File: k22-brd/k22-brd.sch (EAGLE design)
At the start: 35 parts, among them J1 61302011121, J2 61302011121, J3 CORTEX_DEBUG_PTH

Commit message: Vetsi text
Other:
- note added: "B PTD4 BTN"
- note added: "L PTD5 LED"
- note added: "R Reset BTN"
- note added: "U USB connector"
- note removed: "PTD4 BTN"
- note removed: "PTD5 LED"
- note removed: "Reset BTN"
- note removed: "USB connector"
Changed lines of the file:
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@@
 <setting verticaltext="up"/>
 </settings>
-<grid distance="0.1" unitdist="inch" unit="inch" style="lines" multiple="1" display="no" altdistance="0.01" altunitdist="inch" altunit="inch"/>
+<grid distance="0.1" unitdist="inch" unit="mm" style="lines" multiple="1" display="no" altdistance="0.01" altunitdist="inch" altunit="inch"/>
 <layers>
 <layer number="1" name="Top" color="4" fill="1" visible="no" active="no"/>
@@
 <sheet>
 <plain>
-<text x="185.42" y="43.18" size="1.778" layer="104">S SWD Connector</text>
-<text x="177.8" y="-25.4" size="1.778" layer="247">PTD5 LED</text>
-<text x="45.72" y="-25.4" size="1.778" layer="247">Reset BTN</text>
-<text x="-68.58" y="76.2" size="1.778" layer="247">USB connector</text>
-<text x="-68.58" y="129.54" size="1.778" layer="247">V Voltage regulator</text>
-<text x="45.72" y="129.54" size="1.778" layer="247">M MCU</text>
-<text x="177.8" y="129.54" size="1.778" layer="247">Connectors</text>
+<text x="185.42" y="43.18" size="2.54" layer="247">S SWD Connector</text>
+<text x="177.8" y="-25.4" size="2.54" layer="247">L PTD5 LED</text>
+<text x="45.72" y="-25.4" size="2.54" layer="247">R Reset BTN</text>
+<text x="-68.58" y="76.2" size="2.54" layer="247">U USB connector</text>
+<text x="-68.58" y="129.54" size="2.54" layer="247">V Voltage regulator</text>
+<text x="45.72" y="129.54" size="2.54" layer="247">M MCU</text>
+<text x="177.8" y="129.54" size="2.54" layer="247">Connectors</text>
 <wire x1="43.18" y1="-20.32" x2="43.18" y2="-53.34" width="0.1524" layer="247"/>
 <wire x1="43.18" y1="-53.34" x2="101.6" y2="-53.34" width="0.1524" layer="247"/>
@@
 <wire x1="106.68" y1="-53.34" x2="167.64" y2="-53.34" width="0.1524" layer="247"/>
 <wire x1="106.68" y1="-20.32" x2="167.64" y2="-20.32" width="0.1524" layer="247"/>
-<text x="109.22" y="-25.4" size="1.778" layer="247">PTD4 BTN</text>
+<text x="109.22" y="-25.4" size="2.54" layer="247">B PTD4 BTN</text>
 <wire x1="175.26" y1="-20.32" x2="175.26" y2="-53.34" width="0.1524" layer="247"/>
 <wire x1="175.26" y1="-53.34" x2="231.14" y2="-53.34" width="0.1524" layer="247"/>

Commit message: overlap, crystal pad, usb pad, bead pad
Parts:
- removed LU1, LU2: 330, rcl:L-EUL2012C
- added FBU1, FBU2: 330, BeagleBone_Black_Wireless:GHI-BASICCOMPONENTS_FB-(INCH)-0805
- USB-C: device Eagle_WR-USB (rev22b):629722000214 -> poli-USB-C:629722000214
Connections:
- net GND: now also FBU2.P$2; no longer LU2.1
- net USB5V: now also FBU1.P$2; no longer LU1.1
- net USBGNDSHIELD: now also FBU2.P$1; no longer LU2.2
- net VBUSCON: now also FBU1.P$1; no longer LU1.2
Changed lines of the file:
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@@
 <setting verticaltext="up"/>
 </settings>
-<grid distance="0.1" unitdist="inch" unit="mm" style="lines" multiple="1" display="no" altdistance="0.01" altunitdist="inch" altunit="inch"/>
+<grid distance="0.1" unitdist="inch" unit="inch" style="lines" multiple="1" display="no" altdistance="0.01" altunitdist="inch" altunit="inch"/>
 <layers>
 <layer number="1" name="Top" color="4" fill="1" visible="no" active="no"/>
@@
 <part name="J1" library="Headers" library_urn="urn:adsk.eagle:library:11687645" deviceset="61302011121" device="" package3d_urn="urn:adsk.eagle:package:11391910/2"/>
 <part name="J2" library="Headers" library_urn="urn:adsk.eagle:library:11687645" deviceset="61302011121" device="" package3d_urn="urn:adsk.eagle:package:11391910/2"/>
-<part name="USB-C" library="Eagle_WR-USB (rev22b)" deviceset="629722000214" device="" package3d_urn="urn:adsk.eagle:package:32827710/4" value="629722000214"/>
-<part name="LU1" library="rcl" library_urn="urn:adsk.eagle:library:334" deviceset="L-EU" device="L2012C" package3d_urn="urn:adsk.eagle:package:23475/2" value="330"/>
-<part name="LU2" library="rcl" library_urn="urn:adsk.eagle:library:334" deviceset="L-EU" device="L2012C" package3d_urn="urn:adsk.eagle:package:23475/2" value="330"/>
+<part name="USB-C" library="poli-USB-C" deviceset="629722000214" device="" package3d_urn="urn:adsk.eagle:package:32827710/4" value="629722000214"/>
 <part name="RU1" library="rcl" library_urn="urn:adsk.eagle:library:334" deviceset="R-EU_" device="R0805" package3d_urn="urn:adsk.eagle:package:23553/2" value="5k1"/>
 <part name="RU2" library="rcl" library_urn="urn:adsk.eagle:library:334" deviceset="R-EU_" device="R0805" package3d_urn="urn:adsk.eagle:package:23553/2" value="5k1"/>
@@
 <part name="U$5" library="vym0038_k22_misc" deviceset="USBLC6-2SC6" device=""/>
 <part name="CU1" library="rcl" library_urn="urn:adsk.eagle:library:334" deviceset="C-EU" device="C0805" package3d_urn="urn:adsk.eagle:package:23617/2" value="&lt;1,10&gt;u"/>
+<part name="FBU1" library="BeagleBone_Black_Wireless" library_urn="urn:adsk.eagle:library:6644236" deviceset="GHI-BASICCOMPONENTS_FB-(INCH)-" device="0805" package3d_urn="urn:adsk.eagle:package:6644355/2" value="330"/>
+<part name="FBU2" library="BeagleBone_Black_Wireless" library_urn="urn:adsk.eagle:library:6644236" deviceset="GHI-BASICCOMPONENTS_FB-(INCH)-" device="0805" package3d_urn="urn:adsk.eagle:package:6644355/2" value="330"/>
 </parts>
 <sheets>
@@
 <attribute name="VALUE" x="-17.78" y="10.16" size="1.6764" layer="96" align="bottom-center"/>
 </instance>
-<instance part="LU1" gate="G$1" x="-33.02" y="50.8" smashed="yes" rot="R270">
-<attribute name="NAME" x="-36.83" y="52.2986" size="1.778" layer="95"/>
-<attribute name="VALUE" x="-36.83" y="47.498" size="1.778" layer="96"/>
-</instance>
-<instance part="LU2" gate="G$1" x="-33.02" y="43.18" smashed="yes" rot="R270">
-<attribute name="NAME" x="-36.83" y="44.6786" size="1.778" layer="95"/>
-<attribute name="VALUE" x="-36.83" y="39.878" size="1.778" layer="96"/>
-</instance>
 <instance part="RU1" gate="G$1" x="2.54" y="50.8" smashed="yes">
 <attribute name="NAME" x="-1.27" y="52.2986" size="1.778" layer="95"/>
@@
 <attribute name="NAME" x="-33.401" y="59.944" size="1.778" layer="95" rot="R90"/>
 <attribute name="VALUE" x="-28.321" y="59.944" size="1.778" layer="96" rot="R90"/>
+</instance>
+<instance part="FBU1" gate="G$1" x="-33.02" y="50.8" smashed="yes">
+<attribute name="NAME" x="-36.195" y="52.705" size="1.778" layer="95"/>
+<attribute name="VALUE" x="-36.195" y="46.99" size="1.778" layer="96"/>
+</instance>
+<instance part="FBU2" gate="G$1" x="-33.02" y="43.18" smashed="yes">
+<attribute name="NAME" x="-36.195" y="45.085" size="1.778" layer="95"/>
+<attribute name="VALUE" x="-36.195" y="39.37" size="1.778" layer="96"/>
 </instance>
 </instances>
@@
 </segment>
 <segment>
-<pinref part="LU2" gate="G$1" pin="1"/>
 <wire x1="-20.32" y1="43.18" x2="-27.94" y2="43.18" width="0.1524" layer="91"/>
 <label x="-25.4" y="43.18" size="1.778" layer="95"/>
+<pinref part="FBU2" gate="G$1" pin="P$2"/>
 </segment>
 <segment>
@@
 </segment>
 <segment>
-<pinref part="LU1" gate="G$1" pin="2"/>
 <wire x1="-45.72" y1="50.8" x2="-38.1" y2="50.8" width="0.1524" layer="91"/>
 <label x="-50.8" y="50.8" size="1.778" layer="95"/>
+<pinref part="FBU1" gate="G$1" pin="P$1"/>
 </segment>
 <segment>
@@
 </segment>
 <segment>
-<pinref part="LU2" gate="G$1" pin="2"/>
 <wire x1="-45.72" y1="43.18" x2="-38.1" y2="43.18" width="0.1524" layer="91"/>
 <label x="-58.42" y="43.18" size="1.778" layer="95"/>
+<pinref part="FBU2" gate="G$1" pin="P$1"/>
 </segment>
 </net>
@@
 <net name="USB5V" class="0">
 <segment>
-<pinref part="LU1" gate="G$1" pin="1"/>
 <wire x1="-27.94" y1="50.8" x2="-20.32" y2="50.8" width="0.1524" layer="91"/>
 <label x="-25.4" y="50.8" size="1.778" layer="95"/>
@@
 <wire x1="-27.94" y1="50.8" x2="-27.94" y2="58.42" width="0.1524" layer="91"/>
 <junction x="-27.94" y="50.8"/>
-</segment>
-<segment>
+<pinref part="FBU1" gate="G$1" pin="P$2"/>
+</segment>
+<segment>

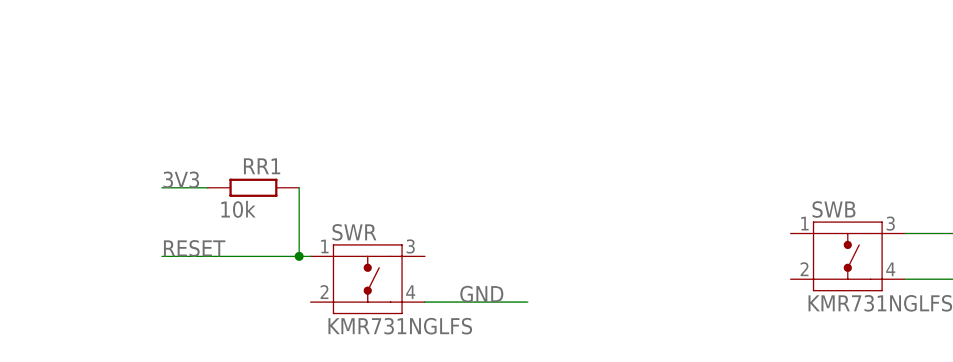
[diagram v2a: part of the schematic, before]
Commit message: oprava textu D4, dimension=3 mil
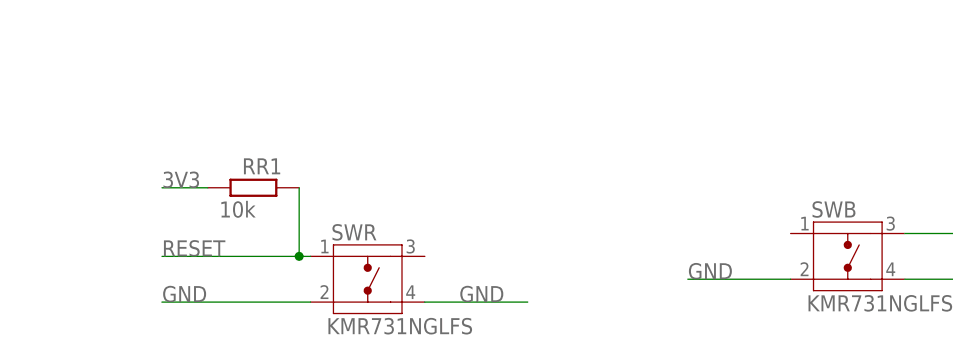
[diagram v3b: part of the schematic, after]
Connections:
- net GND: now also SWB.2, SWR.2
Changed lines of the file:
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@@
 <label x="-45.72" y="58.42" size="1.778" layer="95"/>
+</segment>
+<segment>
+<pinref part="SWB" gate="G$1" pin="2"/>
+<wire x1="123.19" y1="-43.18" x2="111.76" y2="-43.18" width="0.1524" layer="91"/>
+<label x="111.76" y="-43.18" size="1.778" layer="95"/>
+</segment>
+<segment>
+<pinref part="SWR" gate="G$1" pin="2"/>
+<wire x1="69.85" y1="-45.72" x2="53.34" y2="-45.72" width="0.1524" layer="91"/>
+<label x="53.34" y="-45.72" size="1.778" layer="95"/>
 </segment>
 </net>
